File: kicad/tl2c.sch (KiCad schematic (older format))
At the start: 22 parts, among them IC101 ATTINY20-X, P101 12VDC, P102 I2C Master, P103 Spare, P104 ISP Header, P105 LED_DRIVER, P106 240VAC, P107 LED_DRIVER, P108 LED_OUT, SW101 TL3315NF160Q

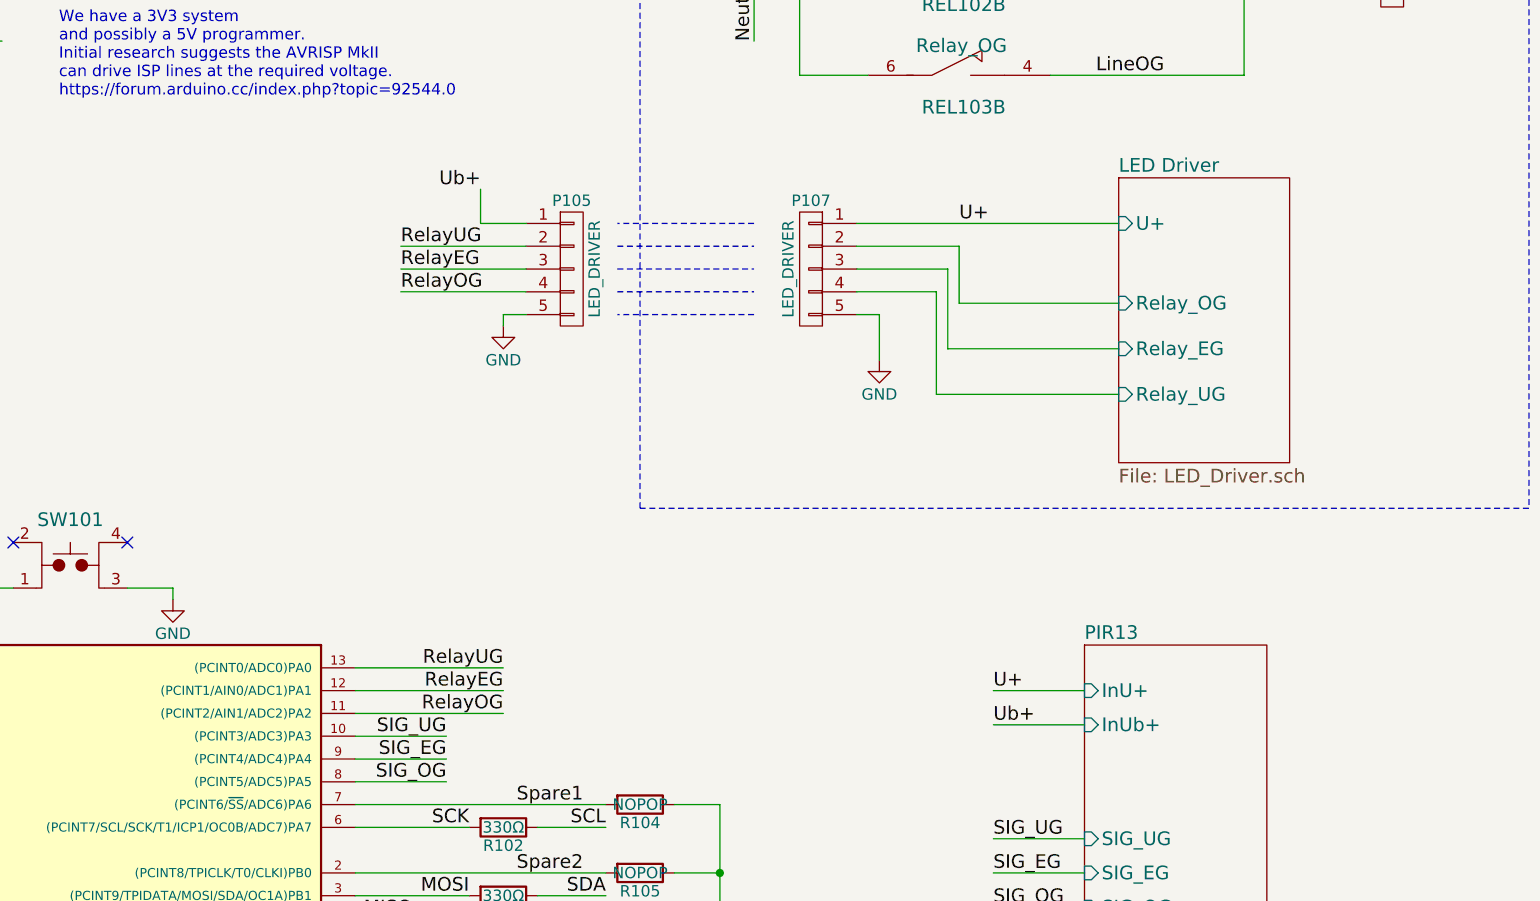
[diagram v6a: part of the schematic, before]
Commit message: Started adding tracks to the layout
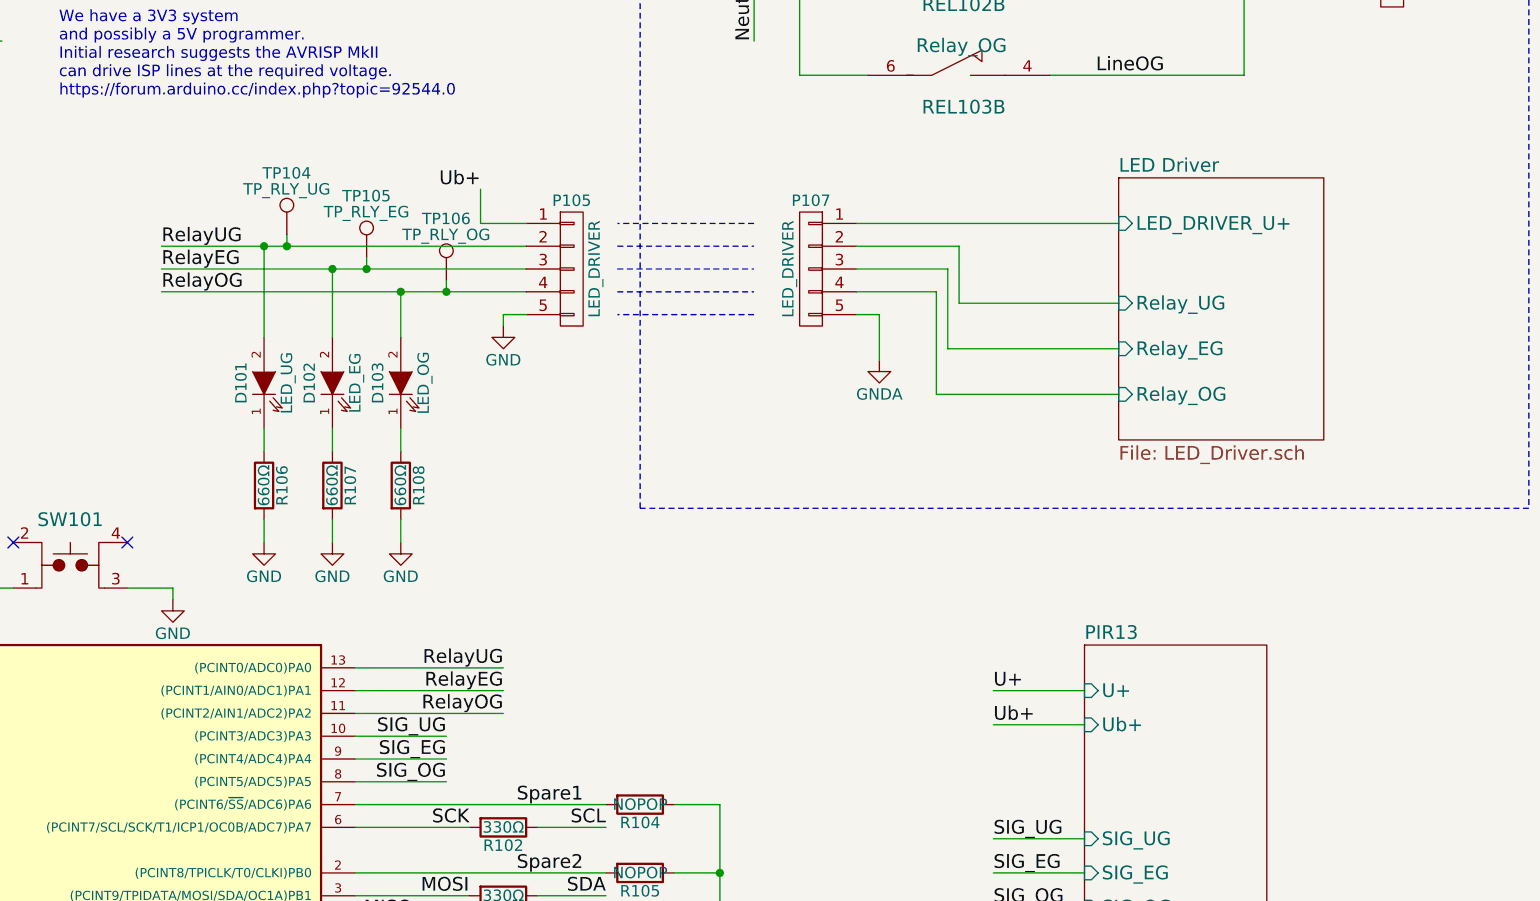
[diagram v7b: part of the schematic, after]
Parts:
- added D101: LED_UG, LEDs:LED_0805, symbol LED
- added D102: LED_EG, LEDs:LED_0805, symbol LED
- added D103: LED_OG, LEDs:LED_0805, symbol LED
- added R106, R107, R108: 660Ω, Resistors_SMD:R_0805, symbol R
- added TP104: TP_RLY_UG, Measurement_Points:Measurement_Point_Round-SMD-Pad_Small, symbol TEST_1P
- added TP105: TP_RLY_EG, Measurement_Points:Measurement_Point_Round-SMD-Pad_Small, symbol TEST_1P
- added TP106: TP_RLY_OG, Measurement_Points:Measurement_Point_Round-SMD-Pad_Small, symbol TEST_1P
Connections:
- net GND: now also R106.2, R107.2, R108.2; no longer P107.5 (P5)
- net LED Driver/Relay_OG: now also P107.4 (P4); no longer P107.2 (P2)
- net LED Driver/Relay_UG: now also P107.2 (P2); no longer P107.4 (P4)
- net RelayEG: now also D102.2 (A), TP105.1
- net RelayOG: now also D103.2 (A), TP106.1
- net RelayUG: now also D101.2 (A), TP104.1
- net U+: no longer P107.1 (P1)
- new net: D101.1 (K), R106.1
- new net: D102.1 (K), R107.1
- new net: D103.1 (K), R108.1
- new net GNDA: P107.5 (P5)
- new net LED Driver/LED_DRIVER_U+: P107.1 (P1)
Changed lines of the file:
@@
 F0 "PIR13" 60
 F1 "PIR13.sch" 60
-F2 "InU+" I L 8600 4700 60
-F3 "InUb+" I L 8600 4850 60
-F4 "SIG_UG" I L 8600 5350 60
-F5 "SIG_EG" I L 8600 5500 60
-F6 "SIG_OG" I L 8600 5650 60
+F2 "SIG_UG" I L 8600 5350 60
+F3 "SIG_EG" I L 8600 5500 60
+F4 "SIG_OG" I L 8600 5650 60
+F5 "U+" I L 8600 4700 60
+F6 "Ub+" I L 8600 4850 60
 $EndSheet
 Text Label 8200 4700 0    60   ~ 0
@@
 SIG_OG
 $Sheet
-S 8750 2450 750  1250
+S 8750 2450 900  1150
 U 585253A2
 F0 "LED Driver" 60
 F1 "LED_Driver.sch" 60
-F2 "Relay_UG" I L 8750 3400 60
+F2 "Relay_UG" I L 8750 3000 60
 F3 "Relay_EG" I L 8750 3200 60
-F4 "Relay_OG" I L 8750 3000 60
-F5 "U+" I L 8750 2650 60
+F4 "Relay_OG" I L 8750 3400 60
+F5 "LED_DRIVER_U+" I L 8750 2650 60
 $EndSheet
-Text Label 8050 2650 0    60   ~ 0
-U+
 Wire Wire Line
 	2600 4600 3100 4600
@@
 	-1   0    0    -1
 $EndComp
+Wire Wire Line
+	7600 3050 7700 3050
+Wire Wire Line
+	7700 3050 7700 3250
 $Comp
 L GND #PWR09
-U 1 1 585418BB
-P 7700 3250
-F 0 "#PWR09" H 7700 3000 50  0001 C CNN
-F 1 "GND" H 7700 3100 50  0000 C CNN
-F 2 "" H 7700 3250 50  0000 C CNN
-F 3 "" H 7700 3250 50  0000 C CNN
-	1    7700 3250
-	1    0    0    -1
-$EndComp
-Wire Wire Line
-	7600 3050 7700 3050
-Wire Wire Line
-	7700 3050 7700 3250
-$Comp
-L GND #PWR010
 U 1 1 58541B90
 P 6050 3100
-F 0 "#PWR010" H 6050 2850 50  0001 C CNN
+F 0 "#PWR09" H 6050 2850 50  0001 C CNN
 F 1 "GND" H 6050 2950 50  0000 C CNN
 F 2 "" H 6050 3100 50  0000 C CNN
@@
 	6650 3900 6650 700
 Wire Wire Line
-	6150 2750 5600 2750
-Wire Wire Line
-	6150 2850 5600 2850
-Wire Wire Line
-	6150 2950 5600 2950
-Text Label 5600 2750 0    60   ~ 0
+	4550 2750 6150 2750
+Wire Wire Line
+	4550 2850 6150 2850
+Wire Wire Line
+	4550 2950 6150 2950
+Text Label 4550 2750 0    60   ~ 0
 RelayUG
-Text Label 5600 2850 0    60   ~ 0
+Text Label 4550 2850 0    60   ~ 0
 RelayEG
-Text Label 5600 2950 0    60   ~ 0
+Text Label 4550 2950 0    60   ~ 0
 RelayOG
 Wire Notes Line
@@
 NoConn ~ 3900 4050
 NoConn ~ 4400 4050
+$Comp
+L LED D101
+U 1 1 5856AA32
+P 5000 3350
+F 0 "D101" H 5000 3450 50  0000 C CNN
+F 1 "LED_UG" H 5000 3250 50  0000 C CNN
+F 2 "LEDs:LED_0805" H 5000 3350 50  0001 C CNN
+F 3 "" H 5000 3350 50  0000 C CNN
+	1    5000 3350
+	0    -1   -1   0
+$EndComp
+$Comp
+L R R106
+U 1 1 5856AB2B
+P 5000 3800
+F 0 "R106" V 5080 3800 50  0000 C CNN
+F 1 "660Ω" V 5000 3800 50  0000 C CNN
+F 2 "Resistors_SMD:R_0805" V 4930 3800 50  0001 C CNN
+F 3 "" H 5000 3800 50  0000 C CNN
+	1    5000 3800
+	1    0    0    -1
+$EndComp
+Wire Wire Line
+	5000 3550 5000 3650
+$Comp
+L GND #PWR010
+U 1 1 5856AF1B
+P 5000 4050
+F 0 "#PWR010" H 5000 3800 50  0001 C CNN
+F 1 "GND" H 5000 3900 50  0000 C CNN
+F 2 "" H 5000 4050 50  0000 C CNN
+F 3 "" H 5000 4050 50  0000 C CNN
+	1    5000 4050
+	1    0    0    -1
+$EndComp
+Wire Wire Line
+	5000 3950 5000 4050
+Wire Wire Line
+	5000 3150 5000 2750
+Connection ~ 5000 2750
+$Comp
+L LED D102
+U 1 1 5856B277
+P 5300 3350
+F 0 "D102" H 5300 3450 50  0000 C CNN
+F 1 "LED_EG" H 5300 3250 50  0000 C CNN
+F 2 "LEDs:LED_0805" H 5300 3350 50  0001 C CNN
+F 3 "" H 5300 3350 50  0000 C CNN
+	1    5300 3350
+	0    -1   -1   0
+$EndComp
+$Comp
+L R R107
+U 1 1 5856B27D
+P 5300 3800
+F 0 "R107" V 5380 3800 50  0000 C CNN
+F 1 "660Ω" V 5300 3800 50  0000 C CNN
+F 2 "Resistors_SMD:R_0805" V 5230 3800 50  0001 C CNN
+F 3 "" H 5300 3800 50  0000 C CNN
+	1    5300 3800
+	1    0    0    -1
+$EndComp
+Wire Wire Line
+	5300 3550 5300 3650
+$Comp
+L GND #PWR011
+U 1 1 5856B284
+P 5300 4050
+F 0 "#PWR011" H 5300 3800 50  0001 C CNN
+F 1 "GND" H 5300 3900 50  0000 C CNN
+F 2 "" H 5300 4050 50  0000 C CNN
+F 3 "" H 5300 4050 50  0000 C CNN
+	1    5300 4050
+	1    0    0    -1
+$EndComp
+Wire Wire Line
+	5300 3950 5300 4050
+Wire Wire Line
+	5300 3150 5300 2850
+Connection ~ 5300 2850
+$Comp
+L LED D103
+U 1 1 5856B503
+P 5600 3350
+F 0 "D103" H 5600 3450 50  0000 C CNN
+F 1 "LED_OG" H 5600 3250 50  0000 C CNN
+F 2 "LEDs:LED_0805" H 5600 3350 50  0001 C CNN
+F 3 "" H 5600 3350 50  0000 C CNN
+	1    5600 3350
+	0    -1   -1   0
+$EndComp
+$Comp
+L R R108
+U 1 1 5856B509
+P 5600 3800
+F 0 "R108" V 5680 3800 50  0000 C CNN
+F 1 "660Ω" V 5600 3800 50  0000 C CNN
+F 2 "Resistors_SMD:R_0805" V 5530 3800 50  0001 C CNN
+F 3 "" H 5600 3800 50  0000 C CNN
+	1    5600 3800
+	1    0    0    -1
+$EndComp
+Wire Wire Line
+	5600 3550 5600 3650
+$Comp
+L GND #PWR012
+U 1 1 5856B510
+P 5600 4050
+F 0 "#PWR012" H 5600 3800 50  0001 C CNN
+F 1 "GND" H 5600 3900 50  0000 C CNN
+F 2 "" H 5600 4050 50  0000 C CNN
+F 3 "" H 5600 4050 50  0000 C CNN
+	1    5600 4050
+	1    0    0    -1
+$EndComp
+Wire Wire Line
+	5600 3950 5600 4050
+Wire Wire Line
+	5600 3150 5600 2950
+Connection ~ 5600 2950
+$Comp
+L GNDA #PWR013
+U 1 1 5856E00B
+P 7700 3250
+F 0 "#PWR013" H 7700 3000 50  0001 C CNN
+F 1 "GNDA" H 7700 3100 50  0000 C CNN
+F 2 "" H 7700 3250 50  0000 C CNN
+F 3 "" H 7700 3250 50  0000 C CNN
+	1    7700 3250
+	1    0    0    -1
+$EndComp
+$Comp
+L TEST_1P TP104
+U 1 1 58571150
+P 5100 2700
+F 0 "TP104" H 5100 2970 50  0000 C CNN
+F 1 "TP_RLY_UG" H 5100 2900 50  0000 C CNN
+F 2 "Measurement_Points:Measurement_Point_Round-SMD-Pad_Small" H 5300 2700 50  0001 C CNN
+F 3 "" H 5300 2700 50  0000 C CNN
+	1    5100 2700
+	1    0    0    -1
+$EndComp
+$Comp
+L TEST_1P TP105
+U 1 1 5857134A
+P 5450 2800
+F 0 "TP105" H 5450 3070 50  0000 C CNN
+F 1 "TP_RLY_EG" H 5450 3000 50  0000 C CNN
+F 2 "Measurement_Points:Measurement_Point_Round-SMD-Pad_Small" H 5650 2800 50  0001 C CNN
+F 3 "" H 5650 2800 50  0000 C CNN
+	1    5450 2800
+	1    0    0    -1
+$EndComp
+$Comp
+L TEST_1P TP106
+U 1 1 585714D0
+P 5800 2900
+F 0 "TP106" H 5800 3170 50  0000 C CNN
+F 1 "TP_RLY_OG" H 5800 3100 50  0000 C CNN
+F 2 "Measurement_Points:Measurement_Point_Round-SMD-Pad_Small" H 6000 2900 50  0001 C CNN
+F 3 "" H 6000 2900 50  0000 C CNN
+	1    5800 2900
+	1    0    0    -1
+$EndComp
+Wire Wire Line
+	5100 2700 5100 2750
+Connection ~ 5100 2750
+Wire Wire Line
+	5450 2800 5450 2850
+Connection ~ 5450 2850
+Wire Wire Line
+	5800 2900 5800 2950
+Connection ~ 5800 2950
 $EndSCHEMATC

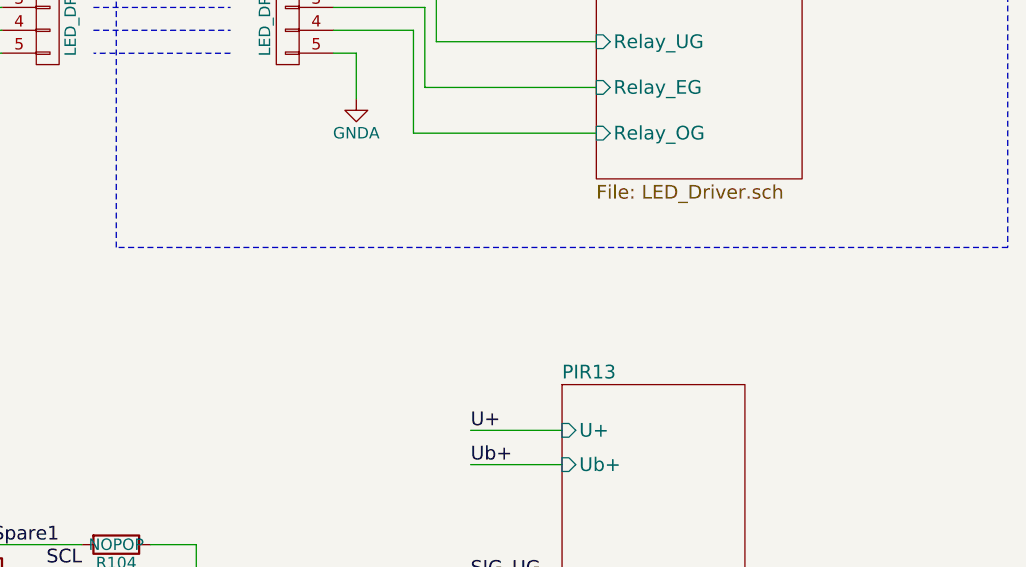
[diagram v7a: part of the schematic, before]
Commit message: A change of heart with some of the parts due to sourcing
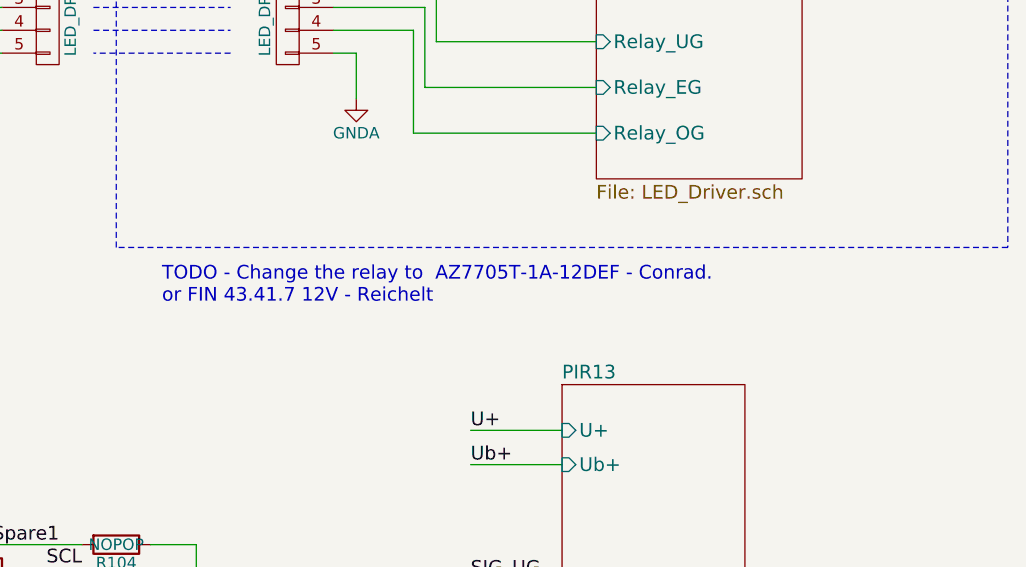
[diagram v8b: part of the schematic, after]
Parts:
- REL101, REL102, REL103: Conrad-PN Value -> 504961 - 62
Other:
- note added: "TODO - Change the relay to AZ7705T-1A-12DEF - Conrad.\nor FIN 43.41.7 12V - Reichelt"
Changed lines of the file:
@@
 F 3 "" H 7920 1140 60  0000 C CNN
 F 4 "JW1AFSN-12-F" H 8050 1150 60  0001 C CNN "MFP"
-F 5 "Value" H 8050 1150 60  0001 C CNN "Conrad-PN"
+F 5 "504961 - 62" H 8050 1150 60  0001 C CNN "Conrad-PN"
 F 6 "Value" H 8050 1150 60  0001 C CNN "Digikey-PN"
 	2    8050 1150
@@
 F 3 "" H 7920 1540 60  0000 C CNN
 F 4 "JW1AFSN-12-F" H 8050 1550 60  0001 C CNN "MFP"
-F 5 "Value" H 8050 1550 60  0001 C CNN "Conrad-PN"
+F 5 "504961 - 62" H 8050 1550 60  0001 C CNN "Conrad-PN"
 F 6 "Value" H 8050 1550 60  0001 C CNN "Digikey-PN"
 	2    8050 1550
@@
 F 3 "" H 7920 1990 60  0000 C CNN
 F 4 "JW1AFSN-12-F" H 8050 2000 60  0001 C CNN "MFP"
-F 5 "Value" H 8050 2000 60  0001 C CNN "Conrad-PN"
+F 5 "504961 - 62" H 8050 2000 60  0001 C CNN "Conrad-PN"
 F 6 "Value" H 8050 2000 60  0001 C CNN "Digikey-PN"
 	2    8050 2000
@@
 	5800 2900 5800 2950
 Connection ~ 5800 2950
+Text Notes 6850 4150 0    60   ~ 0
+TODO - Change the relay to  AZ7705T-1A-12DEF - Conrad.\nor FIN 43.41.7 12V - Reichelt
 $EndSCHEMATC
